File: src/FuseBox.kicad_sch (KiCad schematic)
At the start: 37 parts, among them K3 FINDER-40.61, Q2 2N7002

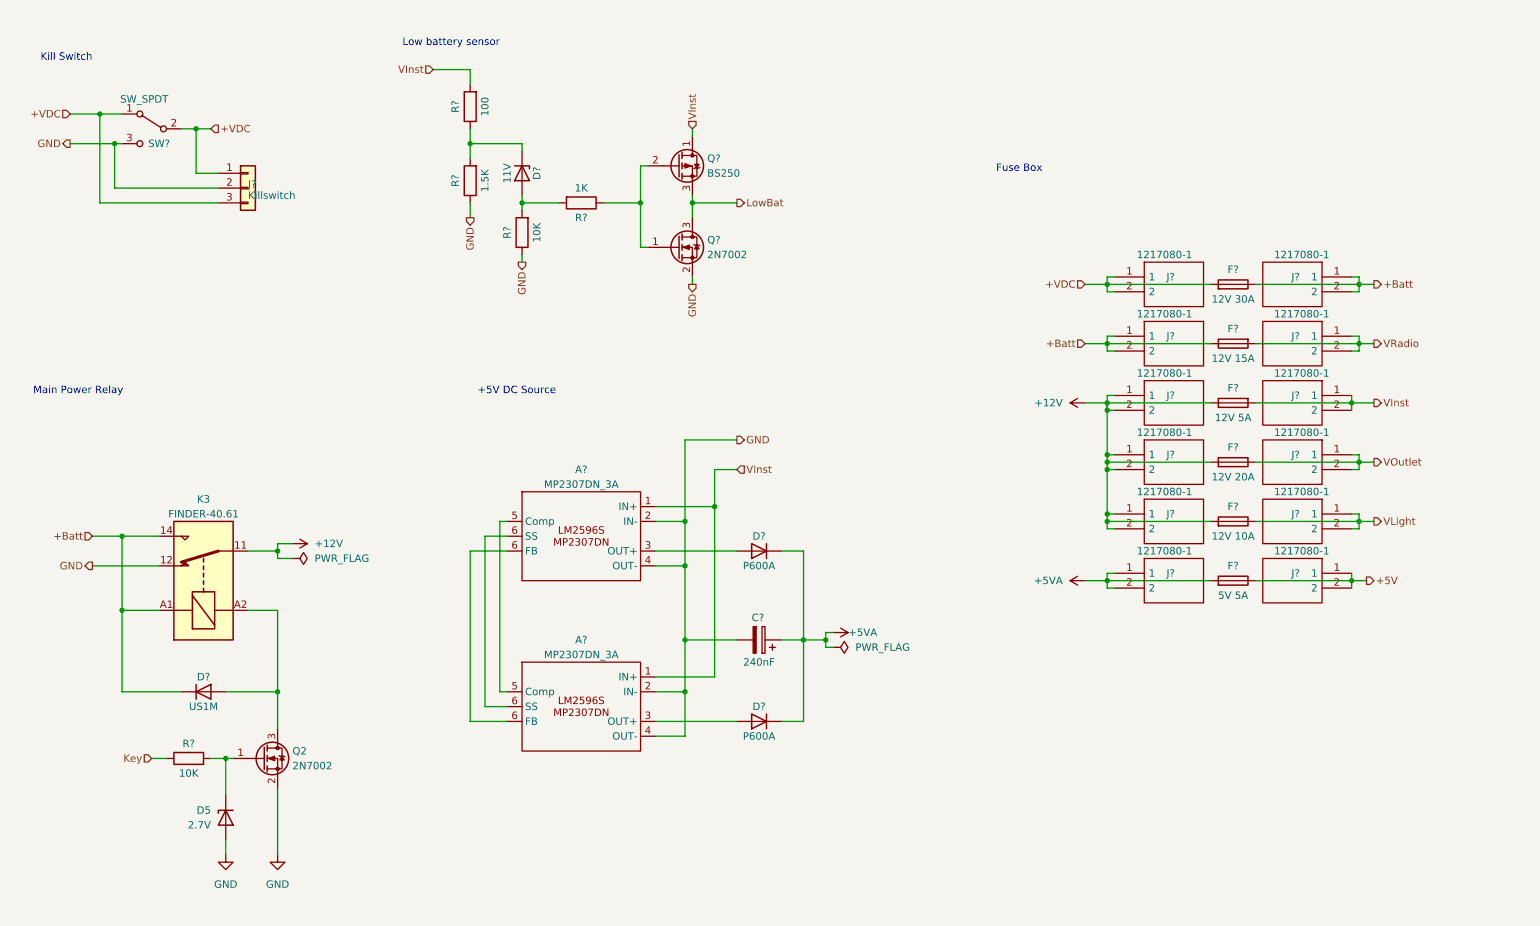
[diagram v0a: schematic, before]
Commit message: Update Schmatics; Cleanup unecessary circuits; Simplify blinkers dimmers; Update PCB; Colorize motorcycle electric diagram.
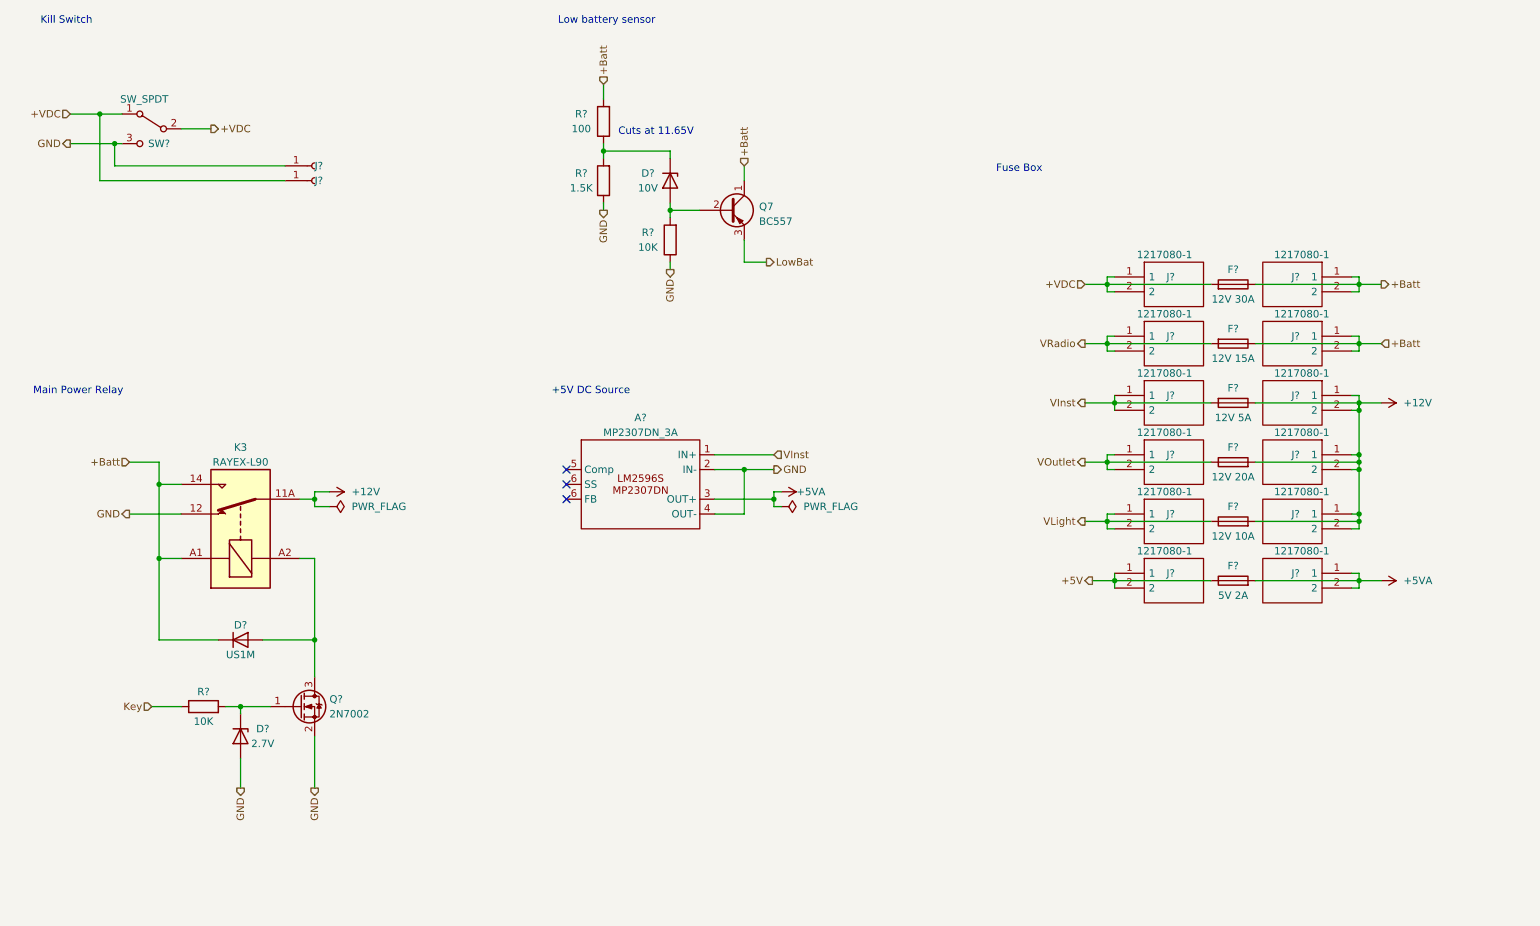
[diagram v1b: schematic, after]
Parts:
- removed A?: MP2307DN_3A, symbol Modules:MP2307DN_3A
- removed C?: 240nF, symbol Device:C_Polarized
- removed D5: 2.7V, Diode_SMD:D_MiniMELF, symbol Diode:BZV55C2V7
- removed D?: P600A, Diode_THT:D_P600_R-6_P12.70mm_Horizontal, symbol Device:D
- removed D?: P600A, symbol Device:D
- removed D?: 11V, Diode_SMD:D_MiniMELF, symbol Diode:BZV55C2V7
- removed J?: Killswitch, symbol Connector_Generic:Conn_01x03
- removed K3: FINDER-40.61, Relay_THT:Relay_DPDT_Finder_40.52, symbol Relay:FINDER-40.51
- removed Q?: BS250, Package_TO_SOT_THT:TO-92_Inline, symbol Transistor_FET:BS250
- removed Q?: 2N7002, Package_TO_SOT_SMD:SOT-23, symbol Transistor_FET:2N7002
- removed R?: 1K, Resistor_SMD:R_1206_3216Metric_Pad1.30x1.75mm_HandSolder, symbol Device:R
- removed R? (x2): 10K, Resistor_SMD:R_1206_3216Metric_Pad1.30x1.75mm_HandSolder, symbol Device:R
- removed R?: 1.5K, Resistor_SMD:R_1206_3216Metric_Pad1.30x1.75mm_HandSolder, symbol Device:R
- removed R?: 100, Resistor_SMD:R_1206_3216Metric_Pad1.30x1.75mm_HandSolder, symbol Device:R
- added D?: 2.7V, Diode_SMD:D_MiniMELF, symbol Diode:BZV55C2V7
- added D?: 10V, Diode_SMD:D_MiniMELF, symbol Diode:BZV55C2V7
- added J? (x2): Conn_01x01_Socket, Connector_Pin:Pin_D1.0mm_L10.0mm, symbol Connector:Conn_01x01_Socket
- added K3: RAYEX-L90, Local Footprints:Relay_SPDT_RAYEX-L90, symbol Relay:RAYEX-L90
- added Q7: BC557, Package_TO_SOT_THT:TO-92_Inline, symbol Transistor_BJT:BC557
- added R?: 1.5K, Resistor_SMD:R_1206_3216Metric_Pad1.30x1.75mm_HandSolder, symbol Device:R
- added R? (x2): 10K, Resistor_SMD:R_1206_3216Metric_Pad1.30x1.75mm_HandSolder, symbol Device:R
- added R?: 100, Resistor_SMD:R_1206_3216Metric_Pad1.30x1.75mm_HandSolder, symbol Device:R
- F?: value 5V 5A -> 5V 2A
- renumbered Q2 to Q?
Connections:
- net +12V: now also K3.11A, K3.11B
- net +5VA: now also A?.3 (OUT+)
- net +Batt: now also K3.14, K3.A1, Q7.1 (C), R?.2
- net +VDC: now also J?.1 (Pin_1)
- net GND: now also D?.2 (A), J?.1 (Pin_1), K3.12, R?.1, R?.1
- net Key: now also R?.1
- net LowBat: now also Q7.3 (E)
- net at D?.2 (A), Q?.3 (D): now also K3.A2
- net at Q?.1 (G): now also D?.1 (K), R?.2
- new net: D?.2 (A), Q7.2 (B), R?.2
- new net: D?.1 (K), R?.1, R?.2
- now unconnected: A?.6 (SS)
- no-connect marks 0 -> 3
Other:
- note added: "Cuts at 11.65V"
- moved on the sheet: A?, D?, F?, J?, Q?

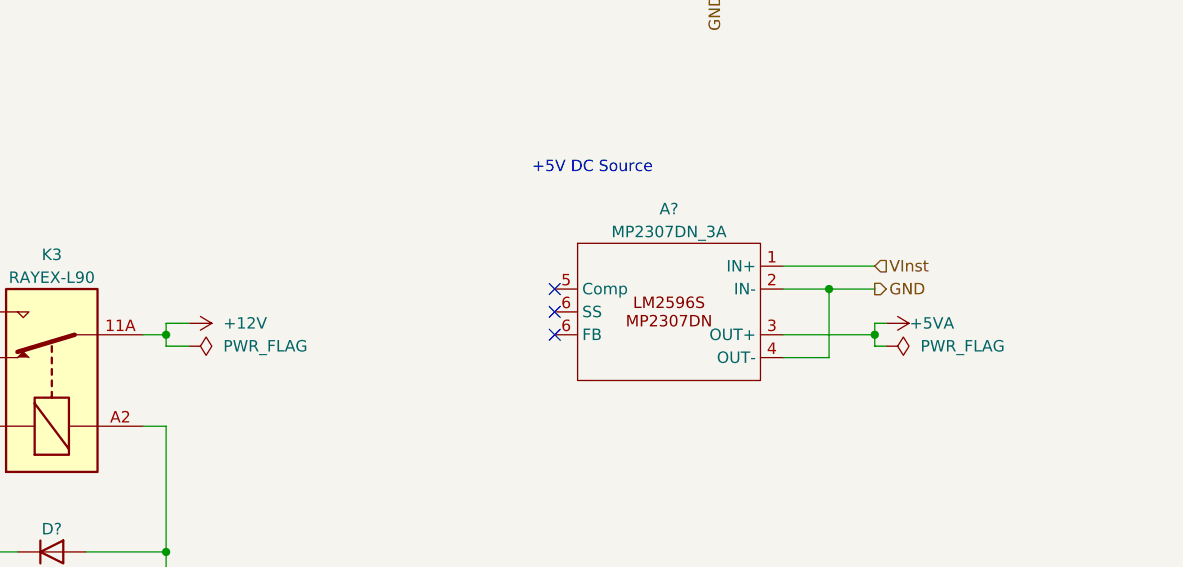
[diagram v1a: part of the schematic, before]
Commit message: Update Schematics; Replace xor with quad nand; Update PCB
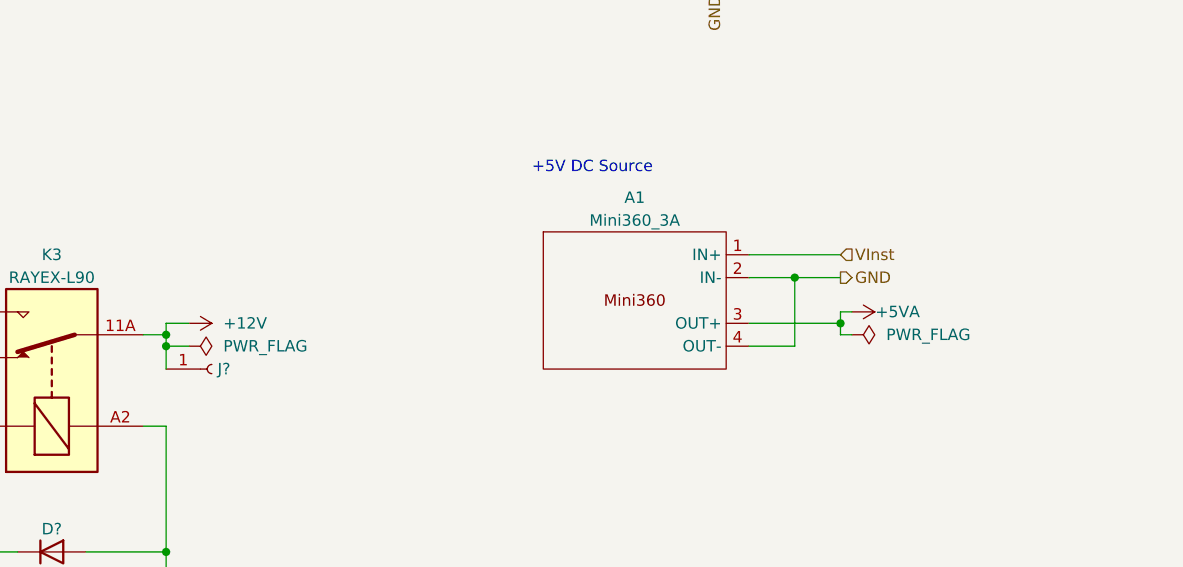
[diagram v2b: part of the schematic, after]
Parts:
- removed A?: MP2307DN_3A, symbol Modules:MP2307DN_3A
- added A1: Mini360_3A, Modules (Custom):Mini360_DC_DC_Buck_Converter, symbol Local Components:Mini360_3A
- added J?: Conn_01x01_Socket, Connector_Pin:Pin_D1.0mm_L10.0mm, symbol Connector:Conn_01x01_Socket
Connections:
- net +12V: now also J?.1 (Pin_1)
- net +5VA: now also A1.3 (OUT+)
- net GND: now also A1.2 (IN-), A1.4 (OUT-)
- net VInst: now also A1.1 (IN+)
- no-connect marks 3 -> 0

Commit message: update mini360 footprint
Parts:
- A1: footprint Modules (Custom):Mini360_DC_DC_Buck_Converter -> Local Footprints:Mini360_DC_DC_Buck_Converter
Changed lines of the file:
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@@
       (effects (font (size 1.27 1.27)))
     )
-    (property "Footprint" "Modules (Custom):Mini360_DC_DC_Buck_Converter" (at 127 105.41 0)
+    (property "Footprint" "Local Footprints:Mini360_DC_DC_Buck_Converter" (at 127 105.41 0)
       (effects (font (size 1.27 1.27)) hide)
     )

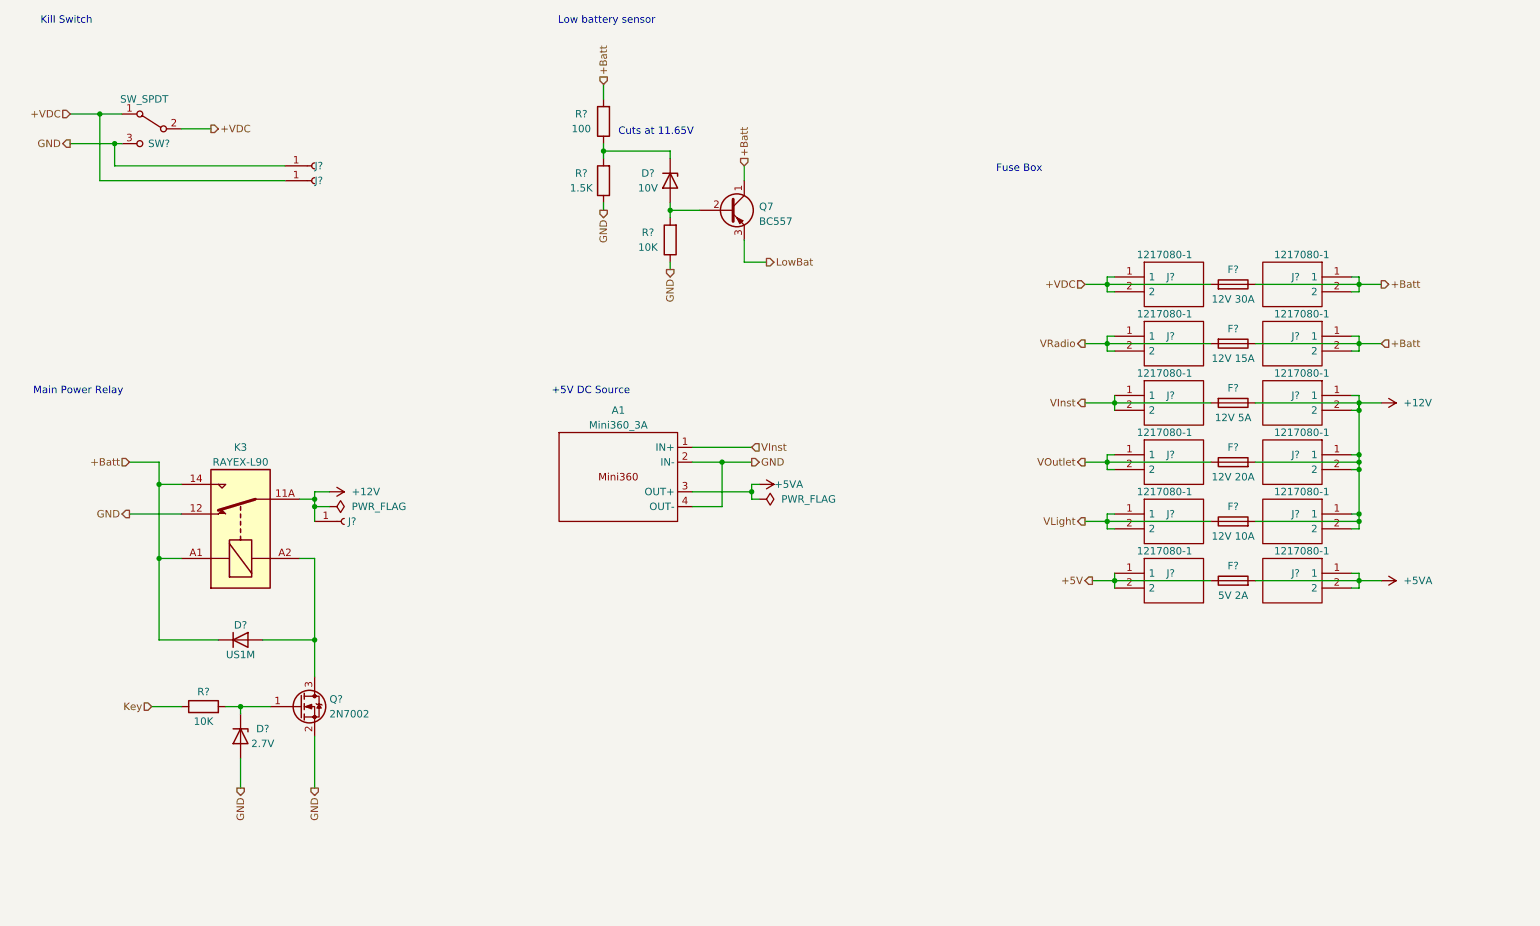
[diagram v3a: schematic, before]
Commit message: simplify circuit diagram. Remove unecessary features; Split board into two components|
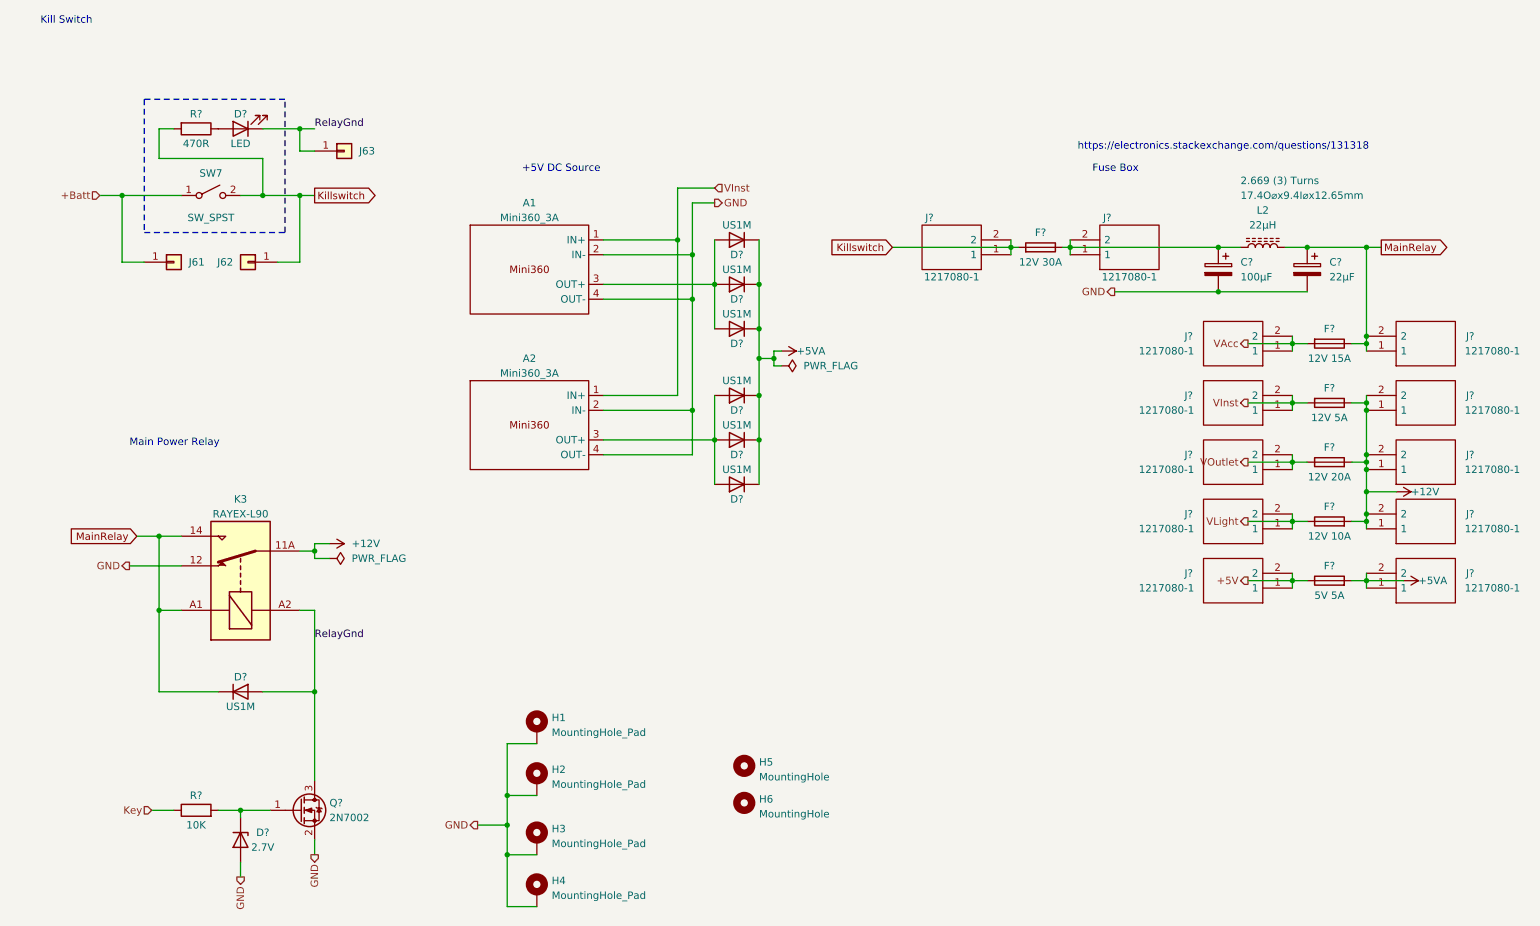
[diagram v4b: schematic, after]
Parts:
- removed D?: 10V, Diode_SMD:D_MiniMELF, symbol Diode:BZV55C2V7
- removed J? (x12): 1217080-1, 1217080-1, symbol SamacSys_Parts:1217080-1
- removed J? (x3): Conn_01x01_Socket, Connector_Pin:Pin_D1.0mm_L10.0mm, symbol Connector:Conn_01x01_Socket
- removed Q7: BC557, Package_TO_SOT_THT:TO-92_Inline, symbol Transistor_BJT:BC557
- removed R?: 1.5K, Resistor_SMD:R_1206_3216Metric_Pad1.30x1.75mm_HandSolder, symbol Device:R
- removed R?: 10K, Resistor_SMD:R_1206_3216Metric_Pad1.30x1.75mm_HandSolder, symbol Device:R
- removed R?: 100, Resistor_SMD:R_1206_3216Metric_Pad1.30x1.75mm_HandSolder, symbol Device:R
- removed SW?: SW_SPDT, symbol Switch:SW_SPDT
- added A2: Mini360_3A, Local Footprints:Mini360_DC_DC_Buck_Converter, symbol Local Components:Mini360_3A
- added C?: 22µF, Capacitor_SMD:C_Elec_6.3x5.4, symbol Device:C_Polarized
- added C?: 100µF, Capacitor_SMD:C_Elec_8x6.2, symbol Device:C_Polarized
- added D? (x6): US1M, Diode_SMD:D_SMA, symbol Diode:US1M
- added D?: LED, symbol Device:LED
- added H1, H2, H3, H4: MountingHole_Pad, MountingHole:MountingHole_3.2mm_M3_DIN965_Pad, symbol Mechanical:MountingHole_Pad
- added H5, H6: MountingHole, MountingHole:MountingHole_5.3mm_M5_Pad_Via, symbol Mechanical:MountingHole
- added J61, J62: Conn_01x01, MountingHole:MountingHole_3.2mm_M3_DIN965_Pad, symbol Connector_Generic:Conn_01x01
- added J63: Conn_01x01, TestPoint:TestPoint_THTPad_D2.5mm_Drill1.2mm, symbol Connector_Generic:Conn_01x01
- added J? (x12): 1217080-1, 1217080-1, symbol SamacSys_Parts:1217080-1
- added L2: 22µH, Inductor_THT:L_Toroid_Vertical_L17.8mm_W9.7mm_P7.11mm_Pulse_B, symbol Device:L_Ferrite
- added R?: 470R, symbol Device:R
- added SW7: SW_SPST, symbol Switch:SW_SPST
- A1: now in the parts list
- D?: footprint Diode_SMD:D_MiniMELF -> Diode_THT:D_DO-35_SOD27_P7.62mm_Horizontal
- F?: value 5V 2A -> 5V 5A
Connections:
- net +12V: now also J?.1, J?.1, J?.1, J?.2, J?.2, J?.2
- net +5V: now also J?.1, J?.2
- net +5VA: now also D?.1 (K), D?.1 (K), D?.1 (K), D?.1 (K), D?.1 (K), D?.1 (K), J?.1, J?.2; no longer A1.3 (OUT+)
- net +Batt: now also J61.1 (Pin_1), SW7.1 (A); no longer D?.1 (K), F?.1, F?.1, K3.14, K3.A1
- net GND: now also A2.2 (IN-), A2.4 (OUT-), C?.2, C?.2, H1.1, H2.1, H3.1, H4.1
- net VInst: now also A2.1 (IN+), J?.1, J?.2
- net VLight: now also J?.1, J?.2
- net VOutlet: now also J?.1, J?.2
- net RelayGnd: now reaches D?.2 (A), K3.A2, Q?.3 (D)
- net RelayGnd: now also D?.1 (K), J63.1 (Pin_1)
- net +VDC renamed Killswitch
- net Killswitch: now also J62.1 (Pin_1), J?.1, J?.2, R?.2, SW7.2 (B)
- net VRadio renamed VAcc
- net VAcc: now also J?.1, J?.2
- new net: A1.3 (OUT+), D?.2 (A), D?.2 (A), D?.2 (A)
- new net: C?.1, F?.1, J?.1, J?.2, L2.1
- new net: D?.2 (A), R?.1
- new net: A2.3 (OUT+), D?.2 (A), D?.2 (A), D?.2 (A)
- new net MainRelay: C?.1, D?.1 (K), F?.1, J?.1, J?.2, K3.14, K3.A1, L2.2
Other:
- note added: "https://electronics.stackexchange.com/questions/131318"
- note removed: "Cuts at 11.65V"
- note removed: "Low battery sensor"
- moved on the sheet: D?, F?, K3, Q?, R?
